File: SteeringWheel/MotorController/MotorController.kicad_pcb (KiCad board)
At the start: 2 copper layers, 55 x 45 mm, 44 parts, among them J1 4P4C, J2 AVR-ISP-10, J3 8P8C, J4 Screw_Terminal_01x02, Q1 Q_NMOS_GSD, SW2 SW_Push, U1 LD1117S50TR_SOT223, U2 MAX485E, U3 ATmega8A-AU, Y1 8Mhz

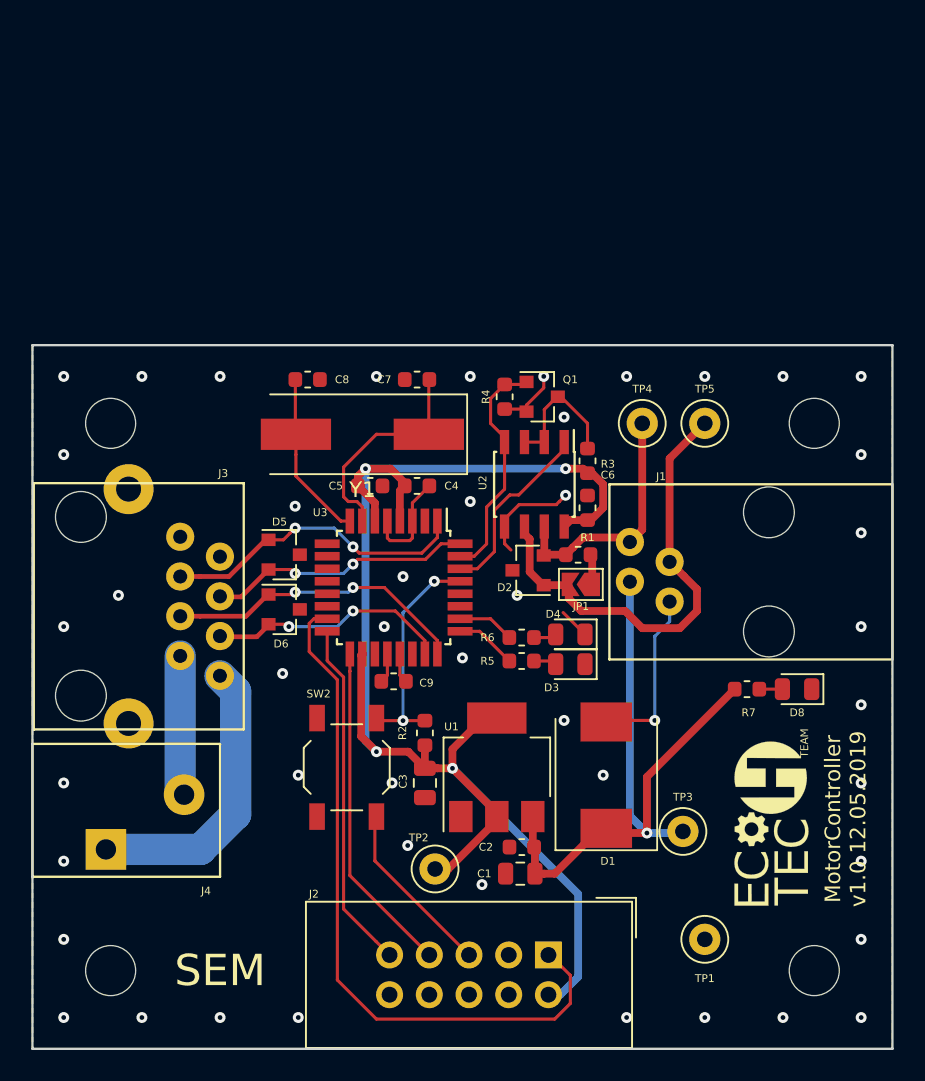
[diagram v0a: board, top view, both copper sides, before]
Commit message: SteeringWheel/: Add layouts for motor controller and connector
Footprints.pretty/: Add molex header, 2x2 connector and AVR

Signed-off-by: Norbert Kamiński <norbert.kaminski@3mdeb.com>
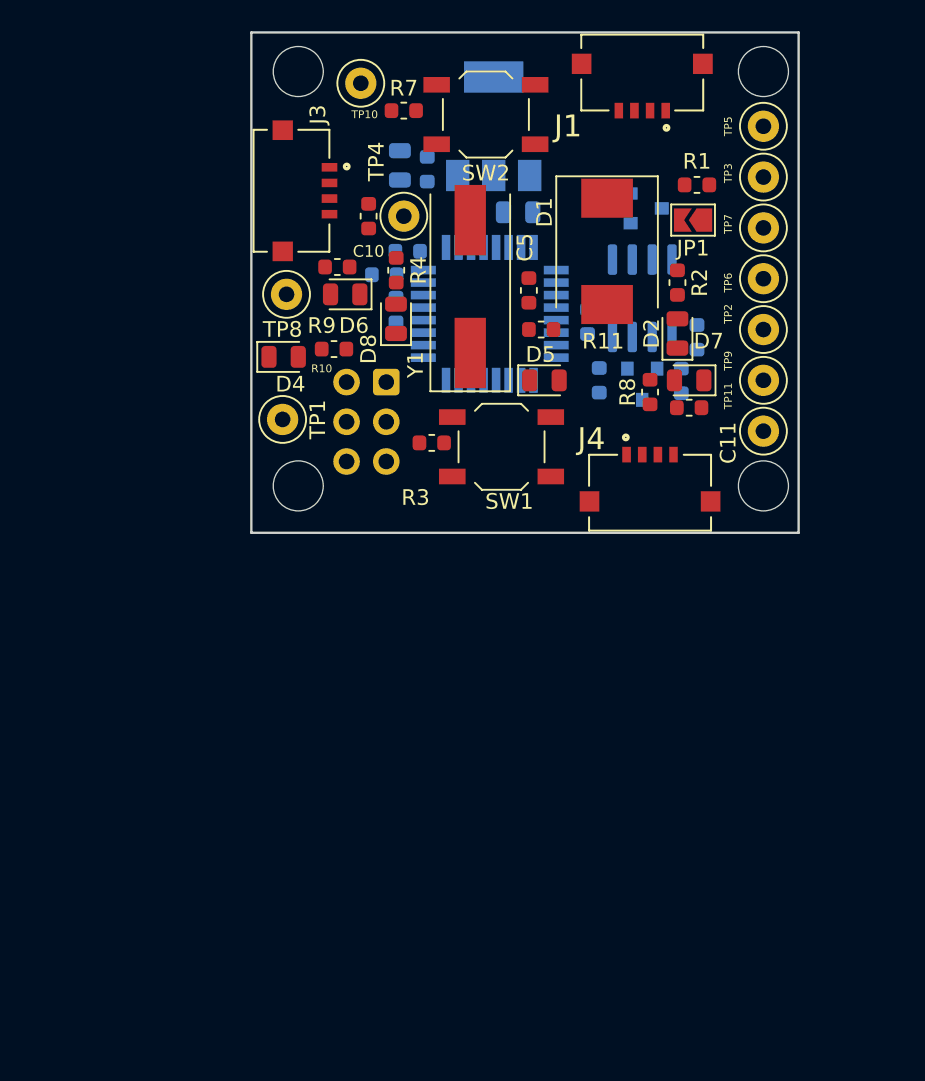
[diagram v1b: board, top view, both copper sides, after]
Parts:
- added C10: 100n, Capacitor_SMD:C_0603_1608Metric, F.Cu at (96.5, 51.8)
- added C11: 100n, Capacitor_SMD:C_0603_1608Metric, F.Cu at (117.0, 64.0)
- added D7: GREEN, LED_SMD:LED_0805_2012Metric, F.Cu at (117.0, 62.2)
- added R10: 1k, Resistor_SMD:R_0603_1608Metric, F.Cu at (94.3, 60.2)
- added R11: 1k, Resistor_SMD:R_0603_1608Metric, F.Cu at (107.5, 59.0)
- added R8: 1k, Resistor_SMD:R_0603_1608Metric, F.Cu at (114.5, 63.0)
- added R9: 1k, Resistor_SMD:R_0603_1608Metric, F.Cu at (94.5, 55.0)
- added SW1: SW_Push, Button_Switch_SMD:SW_SPST_TL3342, F.Cu at (105.0, 66.5)
- added TP10: TestPoint, TestPoint:TestPoint_Loop_D1.80mm_Drill1.0mm_Beaded, F.Cu at (96.0, 43.2)
- added TP11: TestPoint, TestPoint:TestPoint_Loop_D1.80mm_Drill1.0mm_Beaded, F.Cu at (121.8, 65.5)
- added TP6: TestPoint, TestPoint:TestPoint_Loop_D1.80mm_Drill1.0mm_Beaded, F.Cu at (121.8, 55.8)
- added TP7: TestPoint, TestPoint:TestPoint_Loop_D1.80mm_Drill1.0mm_Beaded, F.Cu at (121.8, 52.5)
- added TP8: TestPoint, TestPoint:TestPoint_Loop_D1.80mm_Drill1.0mm_Beaded, F.Cu at (91.2, 56.8)
- added TP9: TestPoint, TestPoint:TestPoint_Loop_D1.80mm_Drill1.0mm_Beaded, F.Cu at (121.8, 62.2)
- C1, C2, C3, C4, C7, C9, G1, Q1: moved to B.Cu
- C6: value 100n -> 22p; moved to B.Cu
- C8: value 22p -> 100n; moved to B.Cu
- D2, D5, D6: value NUP2105L -> GREEN; footprint Package_TO_SOT_SMD:SOT-23 -> LED_SMD:LED_0805_2012Metric
- D3: value RED -> NUP2105L; footprint LED_SMD:LED_0805_2012Metric -> Package_TO_SOT_SMD:SOT-23; moved to B.Cu
- D4: value GREEN -> RED
- J1: value 4P4C -> Molex 1x4; footprint Footprints:4P4C -> Footprints:MOLEX_5037630491
- J2: footprint Connector_IDC:IDC-Header_2x05_P2.54mm_Vertical -> Footprints:AVR-ISP-6; moved to B.Cu
- J3: value 8P8C -> Molex 1x4; footprint Footprints:MTJ-88GX1-FSD -> Footprints:MOLEX_5037630491
- J4: value Screw_Terminal_01x02 -> Molex 1x4; footprint Footprints:TerminalBlock_DG250_02P -> Footprints:MOLEX_5037630491
- R2: value 10k -> 2k
- R4: value 10k -> 1k
- R5, R6: value 1k -> 10k; moved to B.Cu
- R7: value 2k -> 10k
- U1: value LD1117S50TR_SOT223 -> ATmega8A-AU; footprint Package_TO_SOT_SMD:SOT-223-3_TabPin2 -> Package_QFP:TQFP-32_7x7mm_P0.8mm; moved to B.Cu
- U2: value MAX485E -> LD1117S50TR_SOT223; footprint Package_SO:SOIC-8_3.9x4.9mm_P1.27mm -> Package_TO_SOT_SMD:SOT-223-3_TabPin2; moved to B.Cu
- U3: value ATmega8A-AU -> MAX485E; footprint Package_QFP:TQFP-32_7x7mm_P0.8mm -> Package_SO:SOIC-8_3.9x4.9mm_P1.27mm; moved to B.Cu
- moved H2 52.0 mm to (121.8, 69.0)
- moved J4 47.8 mm to (114.5, 67.0), turned to 0 degrees
- moved C1 45.9 mm to (98.5, 48.5), turned to 270 degrees
- moved G1 45.6 mm to (114.0, 45.8), turned to 0 degrees
- moved H4 45.3 mm to (92.0, 69.0)
- moved C2 43.8 mm to (100.2, 48.8), turned to 270 degrees
- moved R7 43.0 mm to (98.8, 45.0)
- moved TP1 42.8 mm to (91.0, 64.8)
- moved SW2 42.7 mm to (104.0, 45.2), turned to 180 degrees
- moved TP3 42.2 mm to (121.8, 49.2)
- moved TP2 40.4 mm to (121.8, 59.0)
- moved C3 37.0 mm to (106.1, 51.5), turned to 0 degrees
- moved J2 35.7 mm to (96.5, 65.2), turned to 180 degrees
- moved D8 34.9 mm to (98.2, 58.3), turned to 90 degrees
- moved D1 33.5 mm to (111.8, 54.0), turned to 270 degrees
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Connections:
- C6 pad 1: +5V -> Net-(C6-Pad1)
- C9 pad 1: Net-(C9-Pad1) -> +5V
- D2 pad 1: /A -> GND
- D2 pad 2: /B -> Net-(D2-Pad2)
- D3 pad 1: GND -> /A
- D3 pad 2: Net-(D3-Pad2) -> /B
- D5 pad 1: /B1 -> GND
- D5 pad 2: /B2 -> Net-(D5-Pad2)
- D6 pad 1: /B3 -> GND
- D6 pad 2: /B4 -> Net-(D6-Pad2)
- J1 pad 1: GND -> /B
- J1 pad 2: +12V -> /A
- J1 pad 3: /A -> +12V
- J1 pad 4: /B -> GND
- J2 pad 1: /MOSI -> /MISO
- J2 pad 3: Net-(J2-Pad3) -> /SCK
- J2 pad 4: GND -> /MOSI
- J3 pad 2: Net-(J3-Pad2) -> /LBTN
- J3 pad 3: /B1 -> /LFR_ADC
- J3 pad 4: /B2 -> +5V
- J4 pad 1: /BH_P -> GND
- J4 pad 2: /BH_N -> /PBTN
- R2 pad 1: +5V -> +12V
- R2 pad 2: /RST -> Net-(D2-Pad2)
- R3 pad 2: Net-(Q1-Pad3) -> /RST
- R4 pad 1: /TX -> +5V
- R4 pad 2: GND -> Net-(D8-Pad2)
- R5 pad 1: /LED_R -> +5V
- R5 pad 2: Net-(D3-Pad2) -> Net-(Q1-Pad3)
- R6 pad 1: /LED_G -> /TX
- R6 pad 2: Net-(D4-Pad2) -> GND
- R7 pad 1: +12V -> +5V
- R7 pad 2: Net-(D8-Pad2) -> Net-(R7-Pad2)
- SW2 pad 1: GND -> Net-(R7-Pad2)
- SW2 pad 2: /RST -> GND
- TP2 pad 1: +5V -> GND
- TP3 pad 1: +12V -> GND
- TP4 pad 1: /B -> +5V
- TP5 pad 1: /A -> +12V
- U1 pad 1: GND -> Net-(U1-Pad1)
- U1 pad 2: +5V -> /LED_R
- U1 pad 3: +12V -> GND
- U2 pad 1: /RX -> GND
- U2 pad 2: Net-(Q1-Pad3) -> +5V
- U2 pad 3: Net-(Q1-Pad3) -> +12V
- U3 pad 1: /B1 -> /RX
- U3 pad 2: Net-(U3-Pad2) -> Net-(Q1-Pad3)
- U3 pad 3: GND -> Net-(Q1-Pad3)
- U3 pad 4: +5V -> /TX
- U3 pad 6: +5V -> /A
- U3 pad 7: Net-(C7-Pad1) -> /B
- U3 pad 8: Net-(C8-Pad1) -> +5V
- Y1 pad 1: Net-(C7-Pad1) -> Net-(C6-Pad1)
- Y1 pad 2: Net-(C8-Pad1) -> Net-(C7-Pad1)
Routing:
- net +5V: track 95.4 -> 0.00 mm, vias 4 -> 0
- net /MOSI: track 44.9 -> 0.00 mm
- net +12V: track 43.3 -> 0.00 mm, vias 1 -> 0
- net GND: track 33.4 -> 0.00 mm, vias 47 -> 0
- net /A: track 29.3 -> 0.00 mm
- net /RST: track 26.0 -> 0.00 mm, vias 2 -> 0
- net /MISO: track 22.4 -> 0.00 mm
- net /SCK: track 21.4 -> 0.00 mm
- net /B1: track 19.9 -> 0.00 mm, vias 2 -> 0
- net /B3: track 19.5 -> 0.00 mm, vias 2 -> 0
- net /BH_P: track 18.5 -> 0.00 mm
- net /B2: track 17.0 -> 0.00 mm, vias 2 -> 0
- net /B: track 15.9 -> 0.00 mm
- net /B4: track 15.5 -> 0.00 mm, vias 2 -> 0
- net /TX: track 14.9 -> 0.00 mm
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- removed copper zone on B.Cu, net GND
- removed copper zone on F.Cu, net GND
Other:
- board size 55 x 45 mm -> 35 x 32 mm
- board text added: "MotorController v2.0 23.05.2020"
- board text removed: "MotorController v1.0 12.05.2019"
